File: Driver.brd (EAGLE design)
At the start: 83.8 x 63.5 mm, 48 parts, among them IC1 L6234D, IC2 7402D, IC3 LM1117MPX-3.3, IC4 TSRN 1-2450, IC5 MAX4373

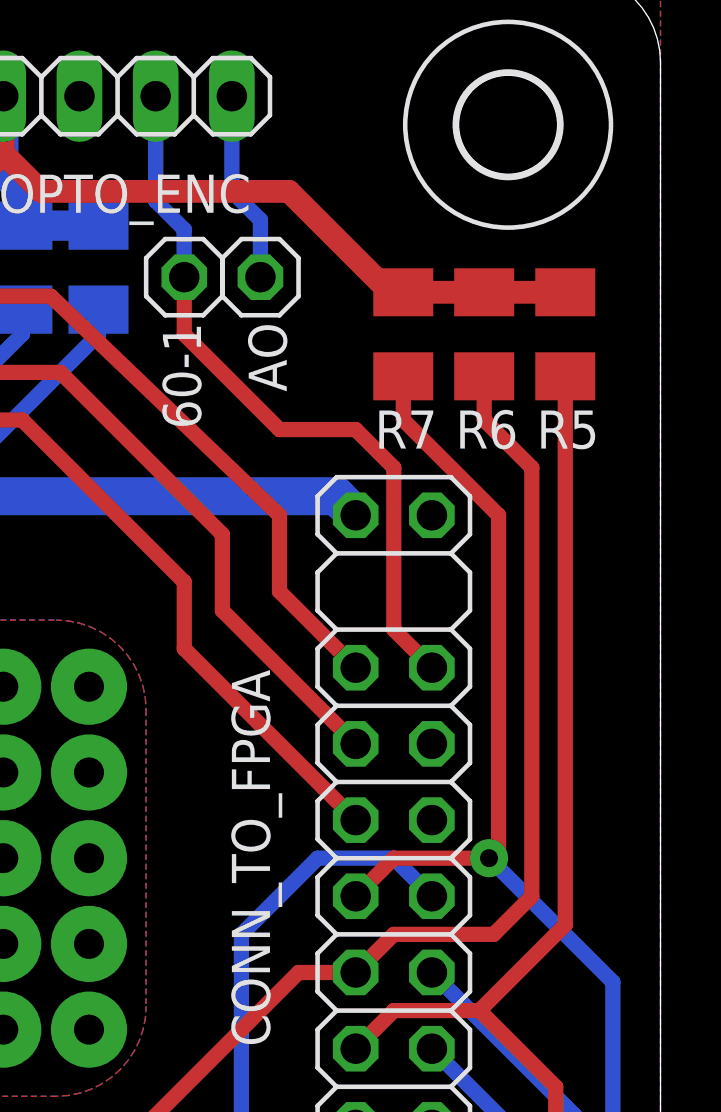
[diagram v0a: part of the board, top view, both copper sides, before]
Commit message: R5..7 change layer
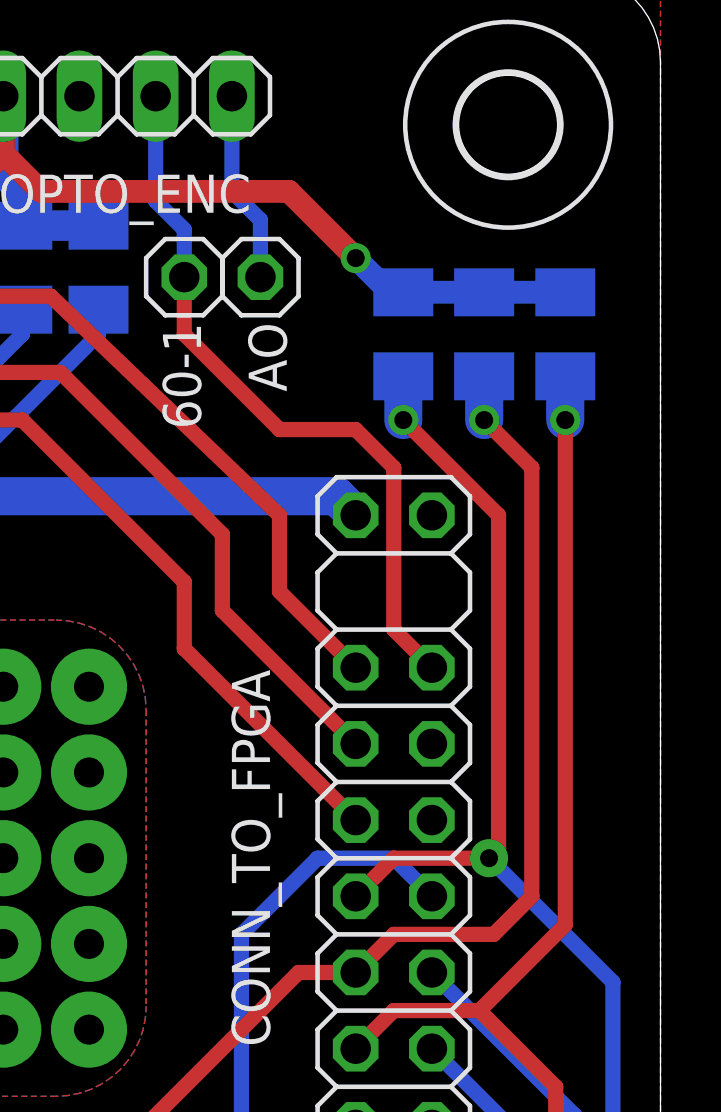
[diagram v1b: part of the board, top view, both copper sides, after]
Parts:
- flipped R5 to the bottom
- flipped R6 to the bottom
- flipped R7 to the bottom
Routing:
- net +3V3: vias 11 -> 12
- net INC: vias 2 -> 3
- net INB: vias 2 -> 3
- net INA: vias 2 -> 3
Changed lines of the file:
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@@
 <attribute name="VALUE" x="50.165" y="13.0175" size="1.27" layer="27" rot="R90"/>
 </element>
-<element name="R5" library="rcl" package="M1206" value="10k" x="80.645" y="51.435" smashed="yes" rot="R270">
-<attribute name="NAME" x="79.6925" y="47.625" size="1.27" layer="25"/>
-<attribute name="VALUE" x="78.105" y="52.705" size="1.27" layer="27" rot="R270"/>
-</element>
-<element name="R6" library="rcl" package="M1206" value="10k" x="77.943075" y="51.435" smashed="yes" rot="R270">
-<attribute name="NAME" x="76.990575" y="47.625" size="1.27" layer="25"/>
-<attribute name="VALUE" x="75.403075" y="52.705" size="1.27" layer="27" rot="R270"/>
-</element>
-<element name="R7" library="rcl" package="M1206" value="10k" x="75.2475" y="51.435" smashed="yes" rot="R270">
-<attribute name="NAME" x="74.295" y="47.625" size="1.27" layer="25"/>
-<attribute name="VALUE" x="72.7075" y="52.705" size="1.27" layer="27" rot="R270"/>
+<element name="R5" library="rcl" package="M1206" value="10k" x="80.645" y="51.435" smashed="yes" rot="MR270">
+<attribute name="NAME" x="81.5975" y="47.625" size="1.27" layer="26" rot="MR0"/>
+<attribute name="VALUE" x="83.185" y="52.705" size="1.27" layer="28" rot="MR270"/>
+</element>
+<element name="R6" library="rcl" package="M1206" value="10k" x="77.943075" y="51.435" smashed="yes" rot="MR270">
+<attribute name="NAME" x="78.895575" y="47.625" size="1.27" layer="26" rot="MR0"/>
+<attribute name="VALUE" x="80.483075" y="52.705" size="1.27" layer="28" rot="MR270"/>
+</element>
+<element name="R7" library="rcl" package="M1206" value="10k" x="75.2475" y="51.435" smashed="yes" rot="MR270">
+<attribute name="NAME" x="76.2" y="47.625" size="1.27" layer="26" rot="MR0"/>
+<attribute name="VALUE" x="77.7875" y="52.705" size="1.27" layer="28" rot="MR270"/>
 </element>
 <element name="R9" library="rcl" package="M1206" value="10k" x="62.23" y="19.3675" smashed="yes" rot="MR270">
@@
 <wire x1="61.9125" y1="57.4675" x2="63.1825" y2="56.1975" width="0.762" layer="1"/>
 <wire x1="63.1825" y1="56.1975" x2="71.4375" y2="56.1975" width="0.762" layer="1"/>
-<wire x1="71.4375" y1="56.1975" x2="75.1175" y2="52.5175" width="0.762" layer="1"/>
-<wire x1="80.645" y1="52.835" x2="77.943075" y2="52.835" width="0.762" layer="1"/>
-<wire x1="77.943075" y1="52.835" x2="75.2475" y2="52.835" width="0.762" layer="1"/>
-<wire x1="75.2475" y1="52.835" x2="75.1175" y2="52.5175" width="0.762" layer="1"/>
+<wire x1="80.645" y1="52.835" x2="77.943075" y2="52.835" width="0.762" layer="16"/>
+<wire x1="77.943075" y1="52.835" x2="75.2475" y2="52.835" width="0.762" layer="16"/>
+<wire x1="75.2475" y1="52.835" x2="75.1175" y2="52.5175" width="0.762" layer="16"/>
 <contactref element="C10" pad="1"/>
 <wire x1="14.9985" y1="13.6525" x2="11.936225" y2="13.6525" width="1.27" layer="16"/>
@@
 <vertex x="24.765" y="12.24915" curve="-90"/>
 </polygon>
+<via x="73.66" y="53.975" extent="1-16" drill="0.6" diameter="0.6"/>
+<wire x1="73.66" y1="53.975" x2="71.4375" y2="56.1975" width="0.762" layer="1"/>
+<wire x1="73.66" y1="53.975" x2="74.8" y2="52.835" width="0.762" layer="16"/>
+<wire x1="74.8" y1="52.835" x2="75.2475" y2="52.835" width="0.762" layer="16"/>
 </signal>
 <signal name="+5V">
@@
 <wire x1="74.93" y1="28.8925" x2="77.7875" y2="28.8925" width="0.508" layer="1"/>
 <wire x1="77.7875" y1="28.8925" x2="80.645" y2="31.75" width="0.508" layer="1"/>
-<wire x1="80.645" y1="31.75" x2="80.645" y2="50.035" width="0.508" layer="1"/>
-<wire x1="80.645" y1="50.165" x2="80.645" y2="50.035" width="0.508" layer="1"/>
+<wire x1="80.645" y1="31.75" x2="80.645" y2="48.5775" width="0.508" layer="1"/>
+<wire x1="80.645" y1="50.165" x2="80.645" y2="50.035" width="0.508" layer="16"/>
 <via x="64.4525" y="6.0325" extent="1-16" drill="0.6" diameter="1.27"/>
 <wire x1="64.4525" y1="6.0325" x2="73.66" y2="15.24" width="0.508" layer="16"/>
@@
 <wire x1="80.3275" y1="16.1925" x2="80.3275" y2="26.3525" width="0.508" layer="1"/>
 <wire x1="80.3275" y1="26.3525" x2="77.7875" y2="28.8925" width="0.508" layer="1"/>
+<via x="80.645" y="48.5775" extent="1-16" drill="0.6" diameter="0.6"/>
+<wire x1="80.645" y1="48.5775" x2="80.645" y2="50.035" width="1.27" layer="16"/>
 </signal>
 <signal name="INB">
@@
 <wire x1="79.530575" y1="32.7025" x2="79.530575" y2="46.99" width="0.508" layer="1"/>
 <wire x1="79.530575" y1="46.99" x2="77.943075" y2="48.5775" width="0.508" layer="1"/>
-<wire x1="77.943075" y1="48.5775" x2="77.943075" y2="50.035" width="0.508" layer="1"/>
+<wire x1="77.943075" y1="48.5775" x2="77.943075" y2="50.035" width="1.27" layer="16"/>
 <via x="50.165" y="21.9075" extent="1-16" drill="0.6" diameter="1.27"/>
 <wire x1="47.625" y1="19.3675" x2="50.165" y2="21.9075" width="0.508" layer="1"/>
@@
 <wire x1="50.165" y1="21.9075" x2="50.165" y2="22.225" width="0.508" layer="16"/>
 <wire x1="50.165" y1="22.225" x2="52.3875" y2="24.4475" width="0.508" layer="16"/>
+<via x="77.943075" y="48.5775" extent="1-16" drill="0.6" diameter="0.6"/>
 </signal>
 <signal name="INA">
@@
 <wire x1="78.4225" y1="34.29" x2="78.4225" y2="45.4025" width="0.508" layer="1"/>
 <wire x1="78.4225" y1="45.4025" x2="75.2475" y2="48.5775" width="0.508" layer="1"/>
-<wire x1="75.2475" y1="48.5775" x2="75.2475" y2="50.035" width="0.508" layer="1"/>
+<wire x1="75.2475" y1="48.5775" x2="75.2475" y2="50.035" width="1.27" layer="16"/>
 <wire x1="66.04" y1="7.3025" x2="67.31" y2="6.0325" width="0.508" layer="1"/>
 <via x="67.31" y="6.0325" extent="1-16" drill="0.6" diameter="1.27"/>
@@
 <wire x1="82.2325" y1="15.24" x2="82.2325" y2="29.845" width="0.508" layer="16"/>
 <wire x1="82.2325" y1="29.845" x2="78.105" y2="33.9725" width="0.508" layer="16"/>
+<via x="75.2475" y="48.5775" extent="1-16" drill="0.6" diameter="0.6"/>
 </signal>
 <signal name="ENC">

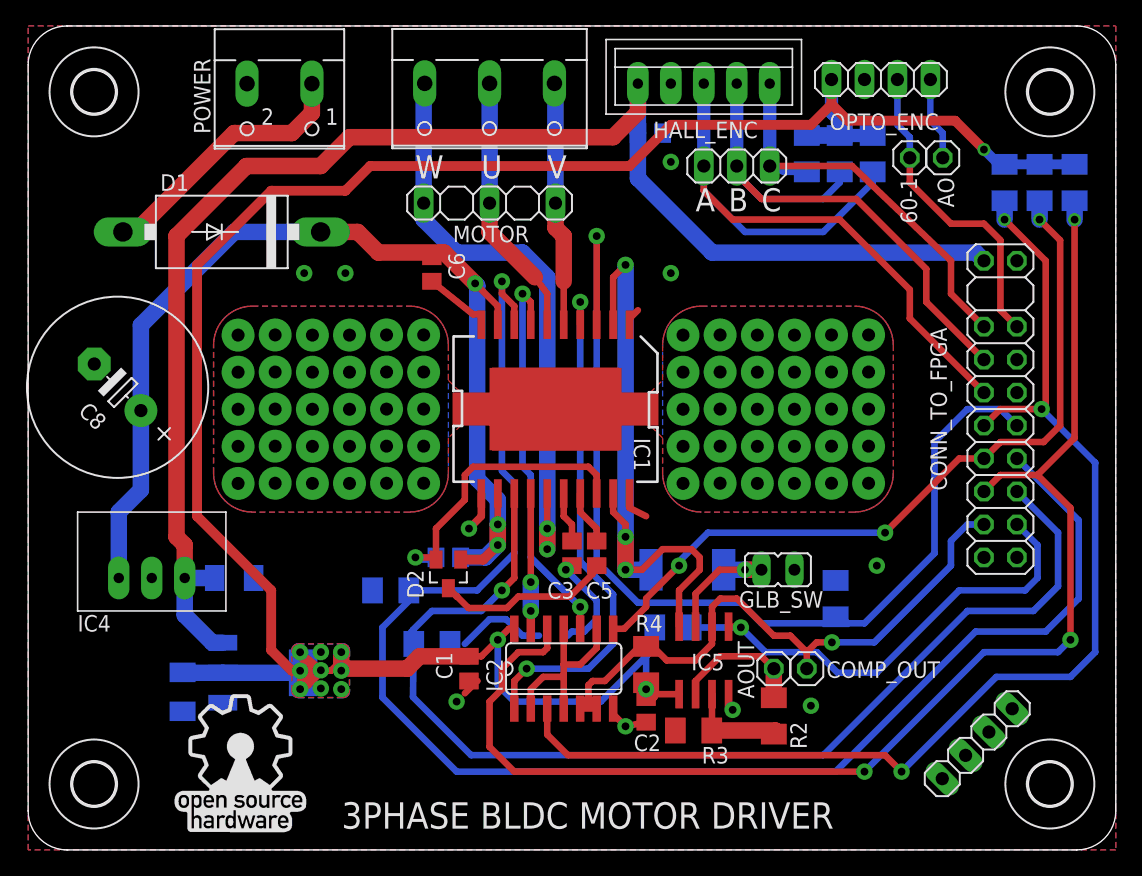
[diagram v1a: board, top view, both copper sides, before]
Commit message: Change on the logic of the Over Current protector
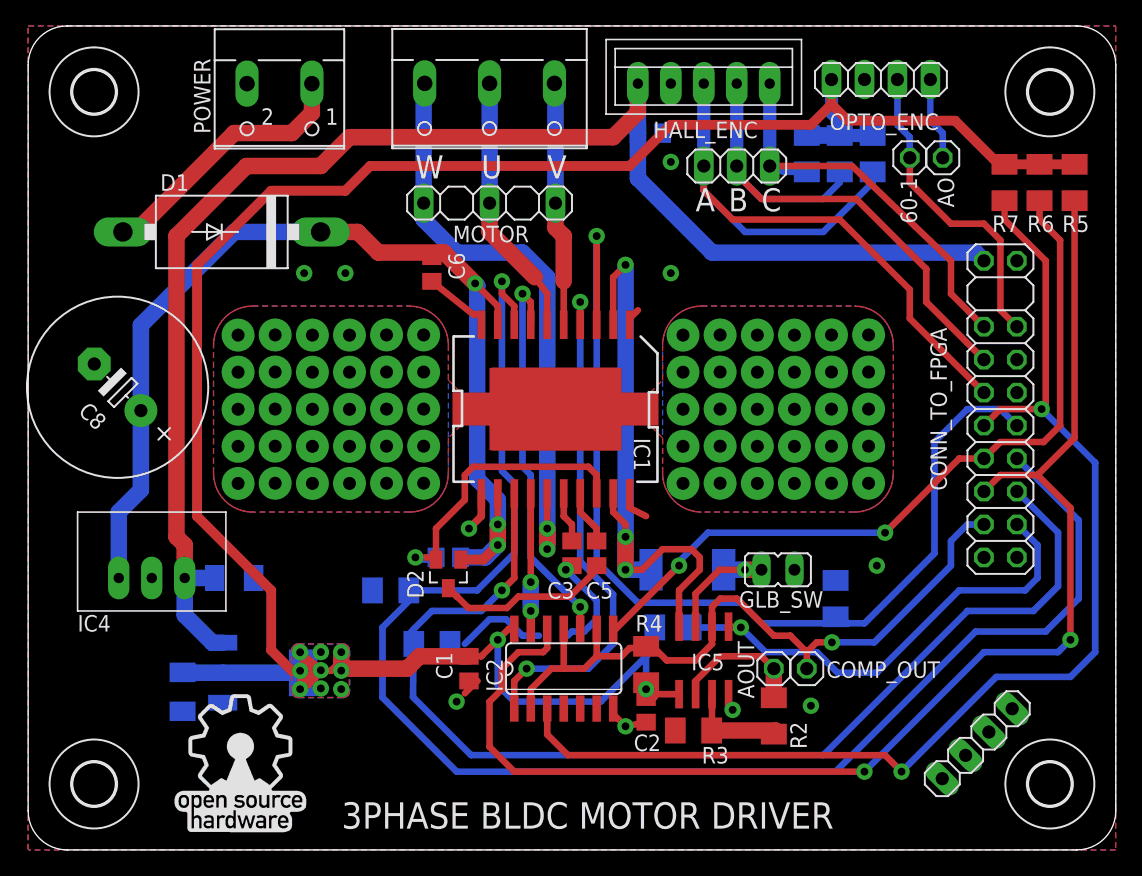
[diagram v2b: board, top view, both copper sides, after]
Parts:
- R4: value 10k -> 1k
- flipped R5 to the top
- flipped R6 to the top
- flipped R7 to the top
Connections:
- removed net N$5: IC2.11, IC2.2, IC2.4, IC2.9
- net COUT: now also IC2.11, IC2.2, IC2.9; no longer IC2.5, IC2.6
- net GND: now also IC2.5, IC2.6
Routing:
- net N$5: track 15.1 -> 0.00 mm
- net COUT: track 49.8 -> 55.5 mm
- net INB: track 59.5 -> 59.1 mm, vias 3 -> 2
- net +3V3: vias 12 -> 11
- net INC: vias 3 -> 2
- net INA: vias 3 -> 2
